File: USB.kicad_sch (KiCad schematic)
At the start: 4 parts, among them J3 USB_C_Receptacle_USB2.0_16P, U2 USBLC6-2SC6

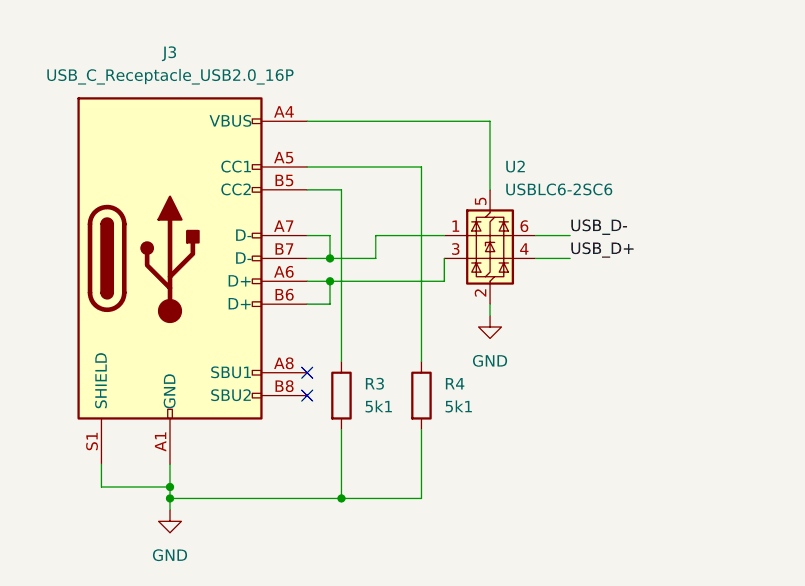
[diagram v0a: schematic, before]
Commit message: fixed some nets
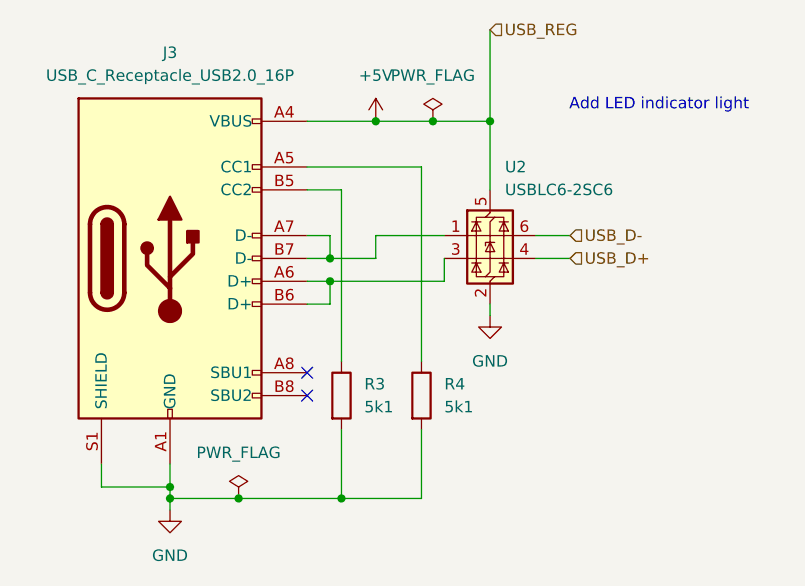
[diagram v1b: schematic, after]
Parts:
- J3: footprint (none) -> Connector_USB:USB_C_Receptacle_GCT_USB4105-xx-A_16P_TopMnt_Horizontal
- R3, R4: footprint (none) -> Resistor_SMD:R_0402_1005Metric
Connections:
- net +5V: now reaches J3.A4 (VBUS), J3.A9 (VBUS), J3.B4 (VBUS), J3.B9 (VBUS), U2.5 (VBUS)
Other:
- note added: "Add LED indicator light"

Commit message: fixed drc error
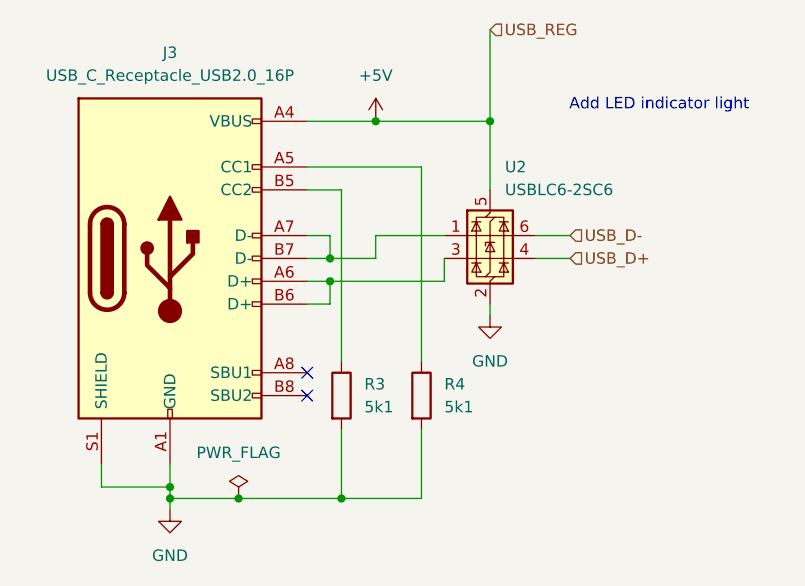
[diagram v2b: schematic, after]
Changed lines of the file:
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@@
-	)
-	(junction
-		(at 175.26 86.36)
-		(diameter 0)
-		(color 0 0 0 0)
 	)
 	(junction
@@
 	(wire
 		(pts
-			(xy 168.91 86.36) (xy 175.26 86.36)
-		)
-		(stroke
-			(width 0)
-			(type default)
-		)
-	)
-	(wire
-		(pts
 			(xy 181.61 76.2) (xy 181.61 86.36)
 		)
@@
 	(wire
 		(pts
-			(xy 175.26 86.36) (xy 181.61 86.36)
+			(xy 168.91 86.36) (xy 181.61 86.36)
 		)
 		(stroke
@@
 					(unit 1)
 				)
-			)
-		)
-	)
-	(symbol
-		(lib_id "power:PWR_FLAG")
-		(at 175.26 86.36 0)
-		(unit 1)
-		(exclude_from_sim no)
-		(in_bom yes)
-		(on_board yes)
-		(dnp no)
-		(fields_autoplaced yes)
-		(property "Reference" "#FLG03"
-			(at 175.26 84.455 0)
-			(effects
-				(font
-					(size 1.27 1.27)
-				)
-				(hide yes)
-			)
-		)
-		(property "Value" "PWR_FLAG"
-			(at 175.26 81.28 0)
-			(effects
-				(font
-					(size 1.27 1.27)
-				)
-			)
-		)
-		(property "Footprint" ""
-			(at 175.26 86.36 0)
-			(effects
-				(font
-					(size 1.27 1.27)
-				)
-				(hide yes)
-			)
-		)
-		(property "Datasheet" "~"
-			(at 175.26 86.36 0)
-			(effects
-				(font
-					(size 1.27 1.27)
-				)
-				(hide yes)
-			)
-		)
-		(property "Description" "Special symbol for telling ERC where power comes from"
-			(at 175.26 86.36 0)
-			(effects
-				(font
-					(size 1.27 1.27)
-				)
-				(hide yes)
-			)
-		)
-		(pin "1"
-		)
-		(instances
-			(project "STM32 Bluetooth Hardware Design"
-				(path "/7294b0c1-22f8-4dfa-8bae-2337522835ff/1e2abb1e-a61e-4f02-b544-b7d6a8e6bbb8"
-					(reference "#FLG03")
-					(unit 1)
-				)
